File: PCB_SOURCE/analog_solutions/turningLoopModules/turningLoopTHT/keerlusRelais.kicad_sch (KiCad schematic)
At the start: 14 parts, among them J1 DCC_out, J2 DCC_IN, J3 Conn_01x03_Male, K1 G5V-2, Q1 BC547, Q101 BC547, U101 LM78L12_TO92

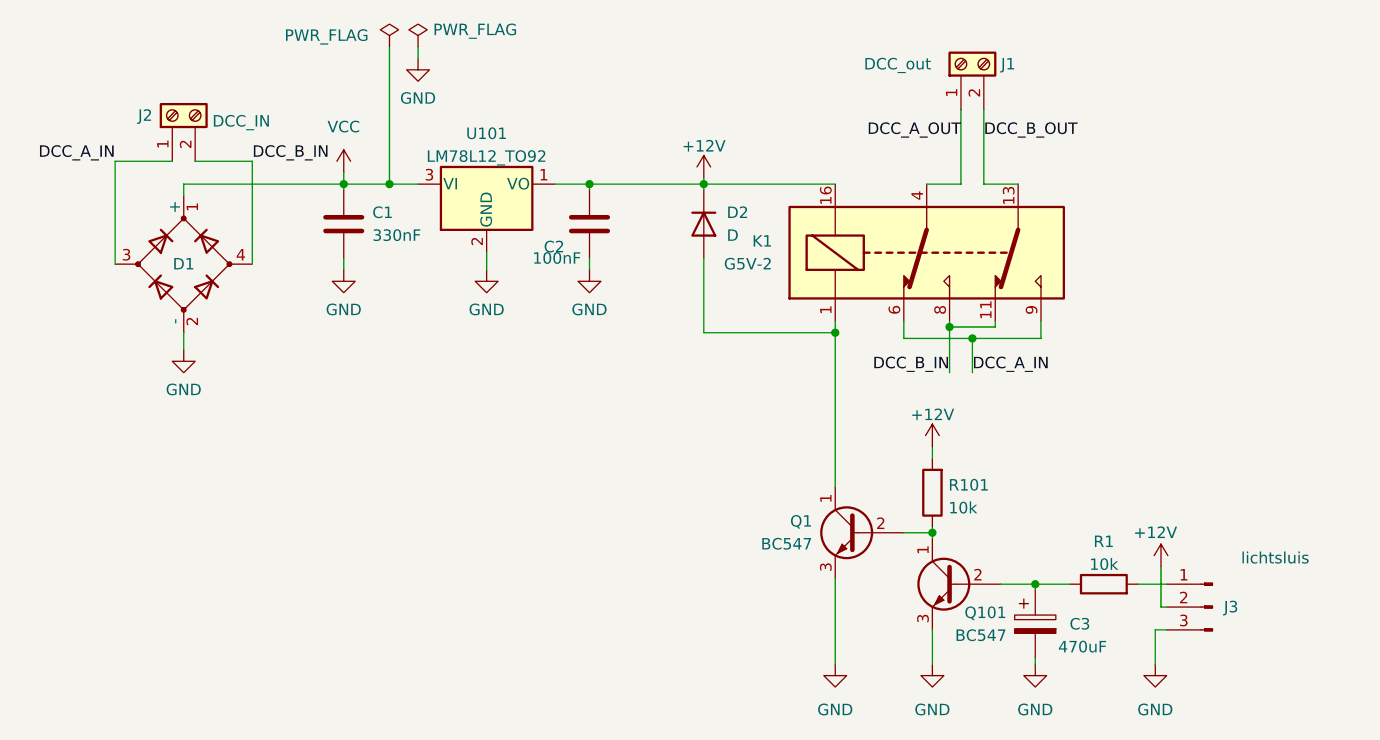
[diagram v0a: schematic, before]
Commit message: Added s88 current sense version, and changed turning loop module THT
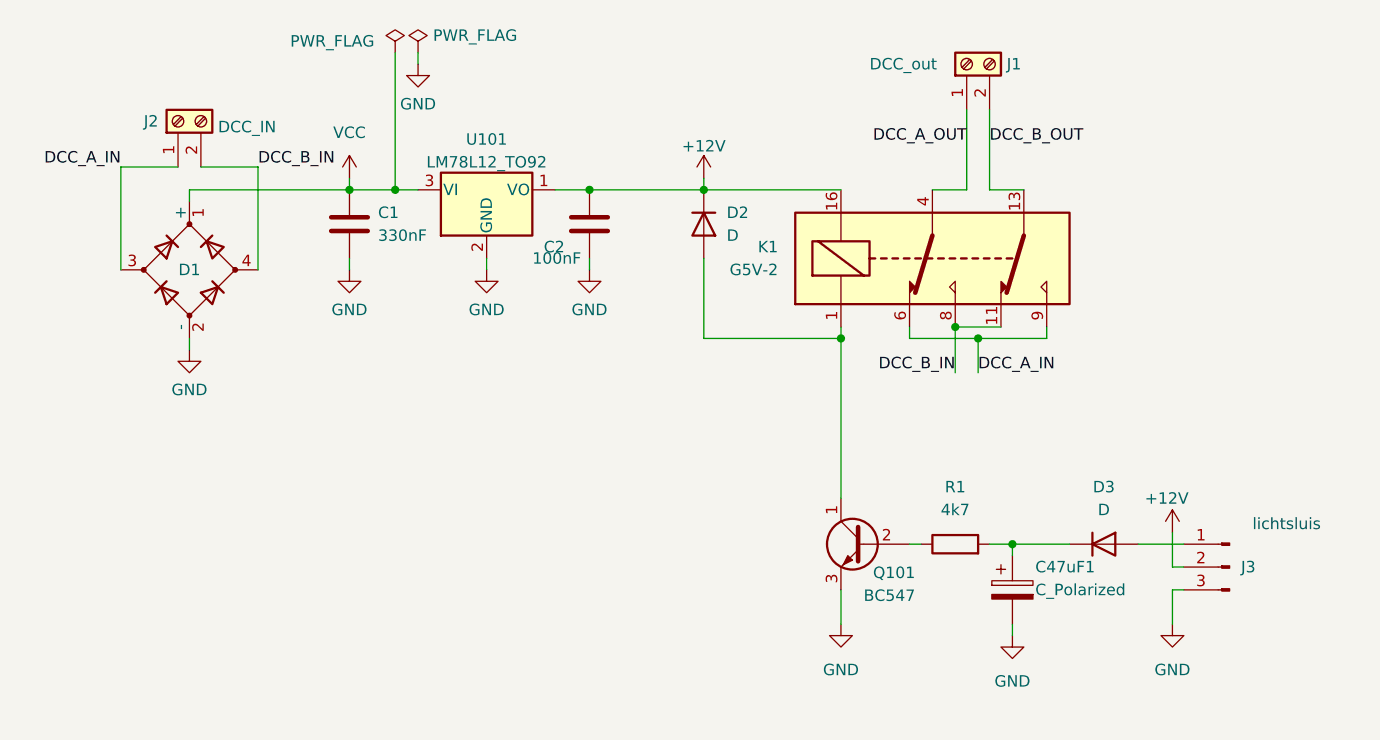
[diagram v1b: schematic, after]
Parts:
- removed C3: 470uF, Capacitor_THT:CP_Radial_D8.0mm_P3.50mm, symbol Device:C_Polarized
- removed Q1: BC547, Package_TO_SOT_THT:TO-92_Inline_Wide, symbol Transistor_BJT:BC547
- removed R101: 10k, Resistor_THT:R_Axial_DIN0207_L6.3mm_D2.5mm_P7.62mm_Horizontal, symbol Device:R
- added C47uF1: C_Polarized, Capacitor_THT:CP_Radial_D4.0mm_P2.00mm, symbol Device:C_Polarized
- added D3: D, Diode_THT:D_DO-34_SOD68_P7.62mm_Horizontal, symbol Device:D
- R1: value 10k -> 4k7
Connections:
- net GND: now also C47uF1.2
- net at Q101.1 (C): now also D2.2 (A), K1.1
- net at J3.1 (Pin_1): now also D3.2 (A); no longer R1.2
- new net: C47uF1.1, D3.1 (K), R1.2
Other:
- moved on the sheet: C1, D1, J1, J2, J3, K1, Q101, R1, U101

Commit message: updated schematic PDF
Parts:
- C3: renamed from C47uF1; value C_Polarized -> 47uF
- renumbered J2 to J1, J1 to J2, Q101 to Q1, U101 to U1
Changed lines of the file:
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@@
 		(dnp no)
 		(fields_autoplaced yes)
-		(property "Reference" "U101"
+		(property "Reference" "U1"
 			(at 138.43 84.5652 0)
 			(effects
@@
 			(project "keerlusRelais"
 				(path "/e957bab8-b860-4d7e-a5c1-615a0849f84a"
-					(reference "U101")
+					(reference "U1")
 					(unit 1)
 				)
@@
 		(dnp no)
 		(fields_autoplaced yes)
-		(property "Reference" "#PWR0109"
+		(property "Reference" "#PWR03"
 			(at 123.19 105.41 0)
 			(effects
@@
 			(project "keerlusRelais"
 				(path "/e957bab8-b860-4d7e-a5c1-615a0849f84a"
-					(reference "#PWR0109")
+					(reference "#PWR03")
 					(unit 1)
 				)
@@
 		(on_board yes)
 		(dnp no)
-		(property "Reference" "#FLG0101"
+		(property "Reference" "#FLG01"
 			(at 128.27 73.025 0)
 			(effects
@@
 			(project "keerlusRelais"
 				(path "/e957bab8-b860-4d7e-a5c1-615a0849f84a"
-					(reference "#FLG0101")
+					(reference "#FLG01")
 					(unit 1)
 				)
@@
 		(dnp no)
 		(fields_autoplaced yes)
-		(property "Reference" "#PWR0104"
+		(property "Reference" "#PWR08"
 			(at 177.8 144.78 0)
 			(effects
@@
 			(project "keerlusRelais"
 				(path "/e957bab8-b860-4d7e-a5c1-615a0849f84a"
-					(reference "#PWR0104")
+					(reference "#PWR08")
 					(unit 1)
 				)
@@
 		(dnp no)
 		(fields_autoplaced yes)
-		(property "Reference" "#PWR0113"
+		(property "Reference" "#PWR07"
 			(at 162.56 92.71 0)
 			(effects
@@
 			(project "keerlusRelais"
 				(path "/e957bab8-b860-4d7e-a5c1-615a0849f84a"
-					(reference "#PWR0113")
+					(reference "#PWR07")
 					(unit 1)
 				)
@@
 		(on_board yes)
 		(dnp no)
-		(property "Reference" "#PWR0103"
+		(property "Reference" "#PWR010"
 			(at 214.63 132.08 0)
 			(effects
@@
 			(project "keerlusRelais"
 				(path "/e957bab8-b860-4d7e-a5c1-615a0849f84a"
-					(reference "#PWR0103")
+					(reference "#PWR010")
 					(unit 1)
 				)
@@
 		(dnp no)
 		(fields_autoplaced yes)
-		(property "Reference" "#PWR0107"
+		(property "Reference" "#PWR05"
 			(at 138.43 105.41 0)
 			(effects
@@
 			(project "keerlusRelais"
 				(path "/e957bab8-b860-4d7e-a5c1-615a0849f84a"
-					(reference "#PWR0107")
+					(reference "#PWR05")
 					(unit 1)
 				)
@@
 		(dnp no)
 		(fields_autoplaced yes)
-		(property "Reference" "#PWR0106"
+		(property "Reference" "#PWR06"
 			(at 149.86 105.41 0)
 			(effects
@@
 			(project "keerlusRelais"
 				(path "/e957bab8-b860-4d7e-a5c1-615a0849f84a"
-					(reference "#PWR0106")
+					(reference "#PWR06")
 					(unit 1)
 				)
@@
 		(on_board yes)
 		(dnp no)
-		(property "Reference" "#FLG0102"
+		(property "Reference" "#FLG02"
 			(at 130.81 73.025 0)
 			(effects
@@
 			(project "keerlusRelais"
 				(path "/e957bab8-b860-4d7e-a5c1-615a0849f84a"
-					(reference "#FLG0102")
+					(reference "#FLG02")
 					(unit 1)
 				)
@@
 		(on_board yes)
 		(dnp no)
-		(property "Reference" "Q101"
+		(property "Reference" "Q1"
 			(at 186.055 132.715 0)
 			(effects
@@
 			(project "keerlusRelais"
 				(path "/e957bab8-b860-4d7e-a5c1-615a0849f84a"
-					(reference "Q101")
+					(reference "Q1")
 					(unit 1)
 				)
@@
 		(dnp no)
 		(fields_autoplaced yes)
-		(property "Reference" "#PWR0102"
+		(property "Reference" "#PWR011"
 			(at 214.63 144.78 0)
 			(effects
@@
 			(project "keerlusRelais"
 				(path "/e957bab8-b860-4d7e-a5c1-615a0849f84a"
-					(reference "#PWR0102")
+					(reference "#PWR011")
 					(unit 1)
 				)
@@
 		(on_board yes)
 		(dnp no)
-		(property "Reference" "J1"
+		(property "Reference" "J2"
 			(at 196.215 76.2 90)
 			(effects
@@
 			(project "keerlusRelais"
 				(path "/e957bab8-b860-4d7e-a5c1-615a0849f84a"
-					(reference "J1")
+					(reference "J2")
 					(unit 1)
 				)
@@
 		(dnp no)
 		(fields_autoplaced yes)
-		(property "Reference" "#PWR0108"
+		(property "Reference" "#PWR02"
 			(at 123.19 92.71 0)
 			(effects
@@
 			(project "keerlusRelais"
 				(path "/e957bab8-b860-4d7e-a5c1-615a0849f84a"
-					(reference "#PWR0108")
+					(reference "#PWR02")
 					(unit 1)
 				)
@@
 		(dnp no)
 		(fields_autoplaced yes)
-		(property "Reference" "#PWR0105"
+		(property "Reference" "#PWR01"
 			(at 105.41 114.3 0)
 			(effects
@@
 			(project "keerlusRelais"
 				(path "/e957bab8-b860-4d7e-a5c1-615a0849f84a"
-					(reference "#PWR0105")
+					(reference "#PWR01")
 					(unit 1)
 				)
@@
 		(dnp no)
 		(fields_autoplaced yes)
-		(property "Reference" "#PWR0110"
+		(property "Reference" "#PWR04"
 			(at 130.81 82.55 0)
 			(effects
@@
 			(project "keerlusRelais"
 				(path "/e957bab8-b860-4d7e-a5c1-615a0849f84a"
-					(reference "#PWR0110")
+					(reference "#PWR04")
 					(unit 1)
 				)
@@
 		(dnp no)
 		(fields_autoplaced yes)
-		(property "Reference" "#PWR0111"
+		(property "Reference" "#PWR09"
 			(at 196.85 146.05 0)
 			(effects
@@
 			(project "keerlusRelais"
 				(path "/e957bab8-b860-4d7e-a5c1-615a0849f84a"
-					(reference "#PWR0111")
+					(reference "#PWR09")
 					(unit 1)
 				)
@@
 		(on_board yes)
 		(dnp no)
-		(property "Reference" "J2"
+		(property "Reference" "J1"
 			(at 100.33 82.55 90)
 			(effects
@@
 			(project "keerlusRelais"
 				(path "/e957bab8-b860-4d7e-a5c1-615a0849f84a"
-					(reference "J2")
+					(reference "J1")
 					(unit 1)
 				)
@@
 		(on_board yes)
 		(dnp no)
-		(property "Reference" "C47uF1"
+		(property "Reference" "C3"
 			(at 199.39 132.08 0)
 			(effects
@@
 			)
 		)
-		(property "Value" "C_Polarized"
+		(property "Value" "47uF"
 			(at 199.39 134.62 0)
 			(effects
@@
 			(project "keerlusRelais"
 				(path "/e957bab8-b860-4d7e-a5c1-615a0849f84a"
-					(reference "C47uF1")
-					(unit 1)
-				)
+					(reference "C3")
+					(unit 1)
+				)
